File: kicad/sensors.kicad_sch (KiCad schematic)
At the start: 52 parts, among them J1 Bus_PCI_Express_x1, J4 Conn_01x02, J6 USB_C_Receptacle_USB2.0_16P, U2 RP2040, U4 W25Q128JVP, U5 BMP388, U8 BNO055, U9 MCP25625T-E/ML, X1 ABM8-272-T3, Y1 ABS07-32.768KHZ-T, Y2 X322516MLB4SI

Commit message: Update board to 0.2.0
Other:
- note added: "Sensor module 0.2.0"
- note removed: "Sensor module 0.1.0"
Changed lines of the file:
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@@
 		)
 	)
-	(text "Sensor module 0.1.0"
+	(text "Sensor module 0.2.0"
 		(exclude_from_sim no)
 		(at 493.014 386.842 0)

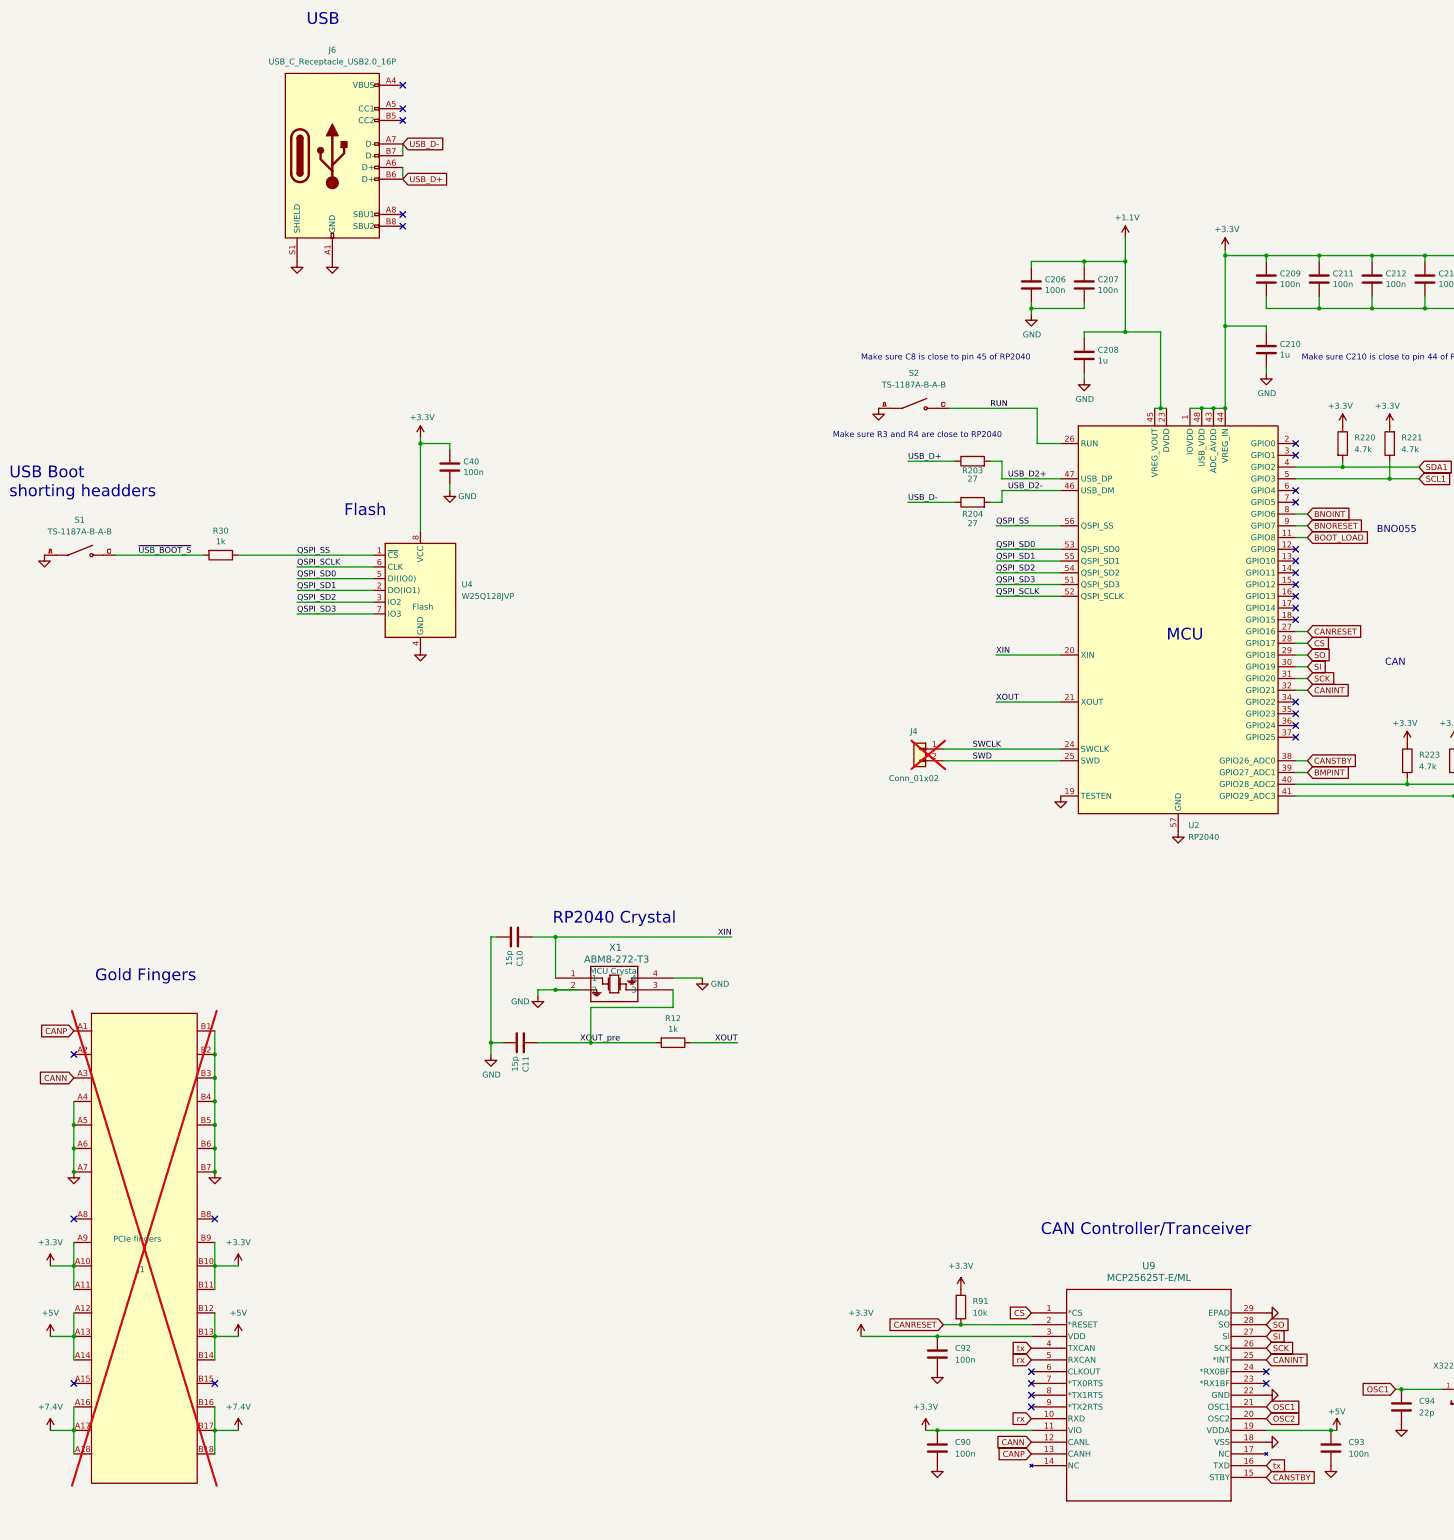
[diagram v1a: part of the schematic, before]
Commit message: add USBC resistors, power status LEDs, silk screen indicator, change SPI pins
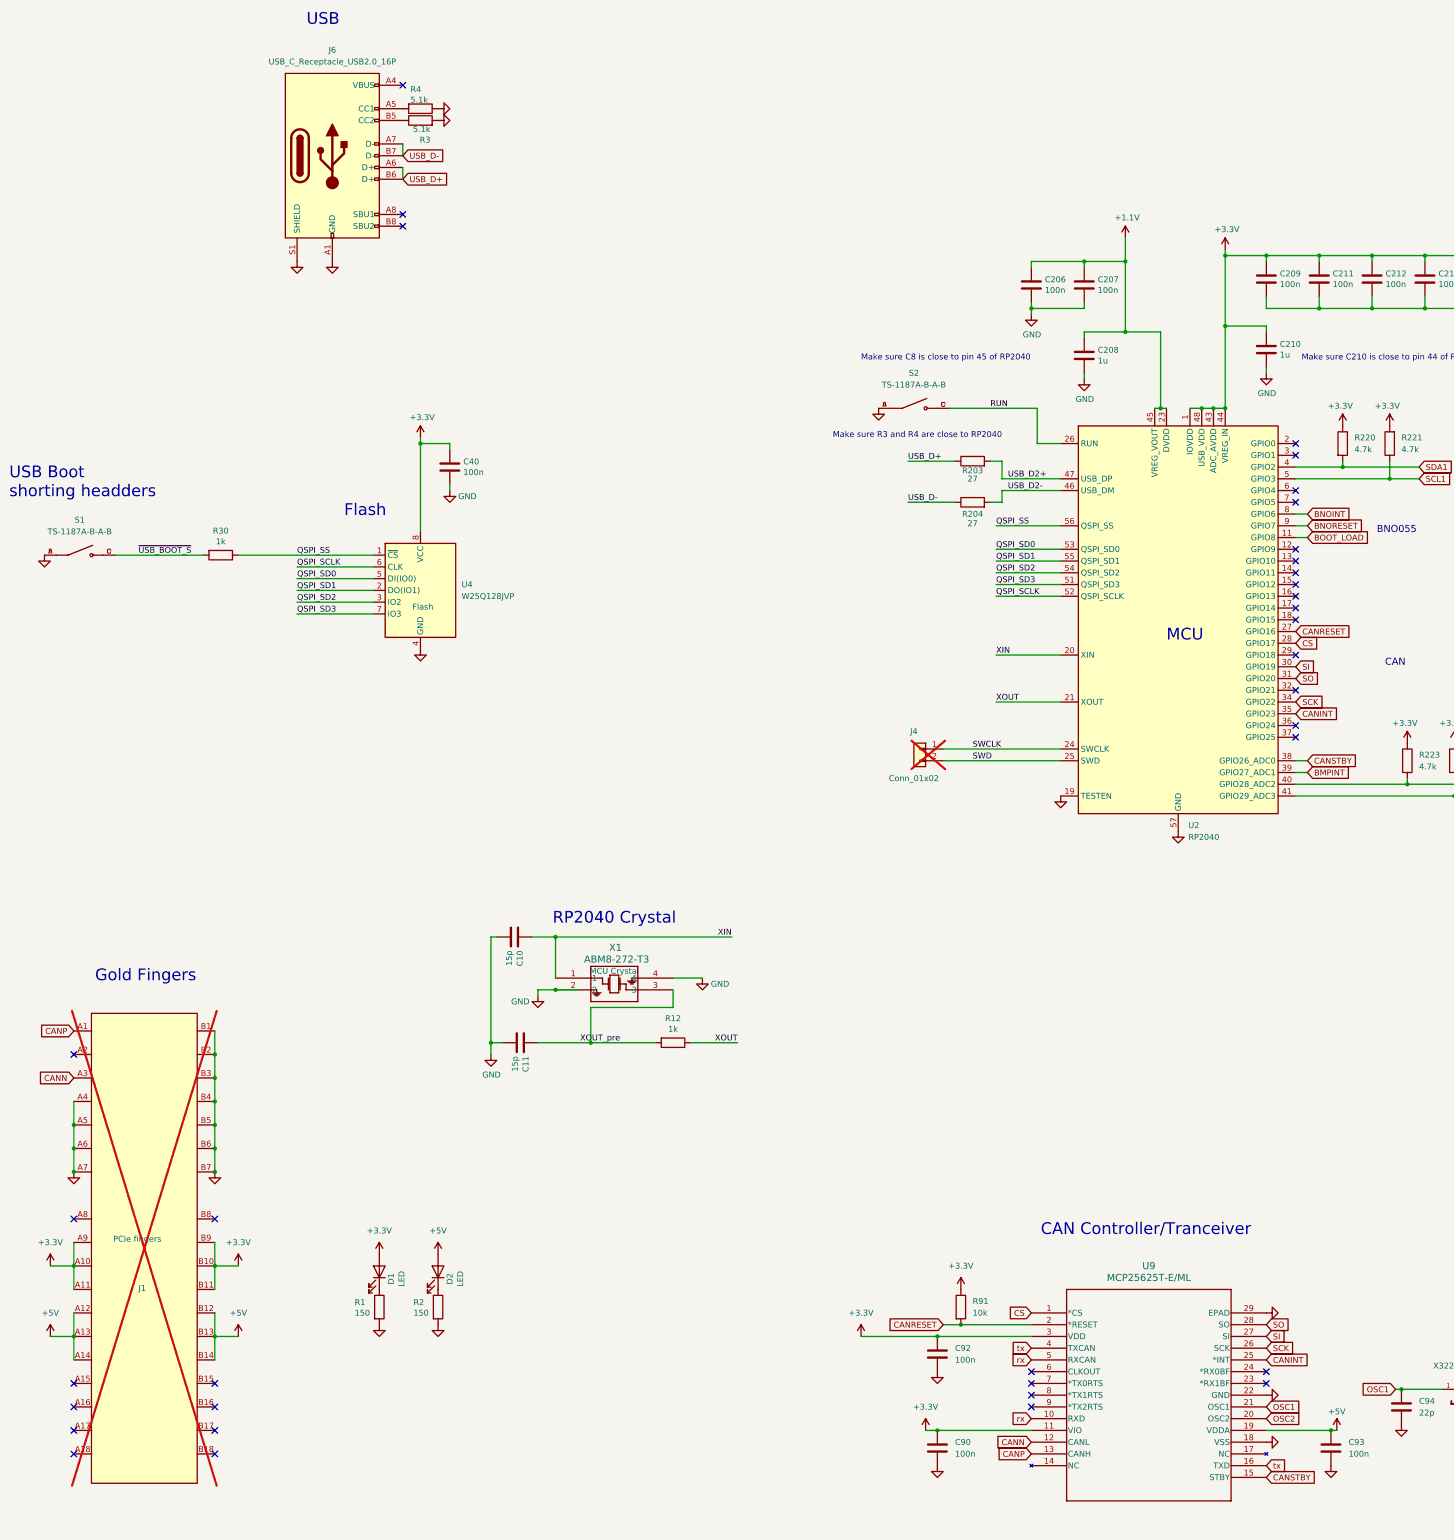
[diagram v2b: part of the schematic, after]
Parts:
- added D1, D2: LED, LED_SMD:LED_0603_1608Metric, symbol Device:LED
- added R1, R2: 150, Resistor_SMD:R_0603_1608Metric, symbol Device:R
- added R3, R4: 5.1k, Resistor_SMD:R_0603_1608Metric, symbol Device:R
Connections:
- net +3.3V: now also D1.2 (A)
- net +5V: now also D2.2 (A)
- net CANINT: now also U2.35 (GPIO23); no longer U2.32 (GPIO21)
- net GND: now also R1.2, R2.2, R3.2, R4.1
- net SCK: now also U2.34 (GPIO22); no longer U2.31 (GPIO20)
- net SO: now also U2.31 (GPIO20); no longer U2.29 (GPIO18)
- net at J6.A5 (CC1): now also R4.2
- net at J6.B5 (CC2): now also R3.1
- removed net +7.4V: J1.A16 (PERp0), J1.A17 (PERn0), J1.A18 (GND), J1.B16 (GND), J1.B17 (~{PRSNT2}), J1.B18 (GND)
- new net: D2.1 (K), R2.1
- new net: D1.1 (K), R1.1
- no-connect marks 31 -> 35

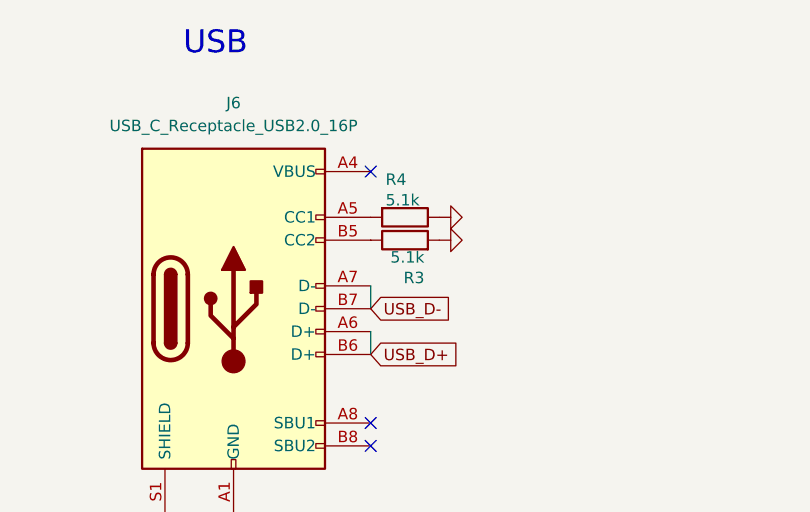
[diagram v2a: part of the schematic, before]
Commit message: update BOM, generate new production files
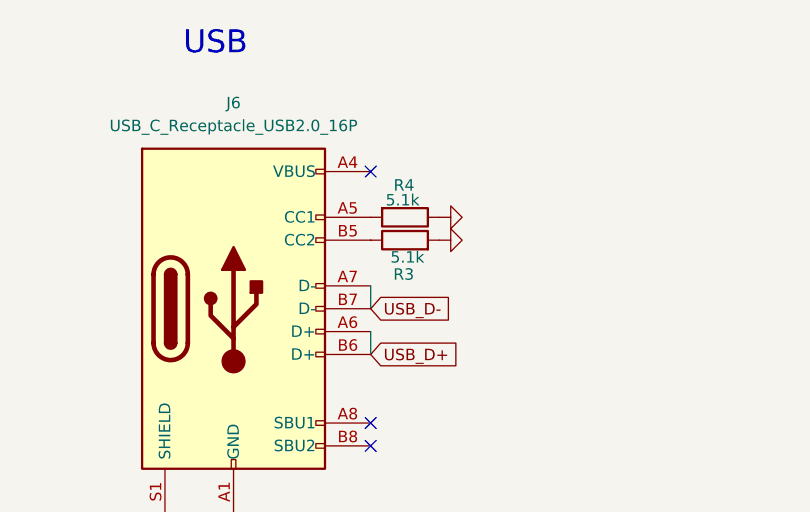
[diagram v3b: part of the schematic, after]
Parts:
- R3, R4: footprint Resistor_SMD:R_0603_1608Metric -> Resistor_SMD:R_0402_1005Metric; JLC Link https://jlcpcb.com/partdetail/23535-0603WAF1500T5E/C22808 -> https://jlcpcb.com/partdetail/26648-0402WGF5101TCE/C25905; LCSC Part # C22808 -> C25905; info 150 ohm -> 5.1k ohm; price C$0.0013 -> C$0.0006
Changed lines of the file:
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@@
 		(dnp no)
 		(property "Reference" "R3"
-			(at 138.049 77.851 90)
+			(at 136.906 77.47 90)
 			(effects
 				(font
@@
 			)
 		)
-		(property "Footprint" "Resistor_SMD:R_0603_1608Metric"
+		(property "Footprint" "Resistor_SMD:R_0402_1005Metric"
 			(at 135.89 75.438 90)
 			(effects
@@
 			)
 		)
-		(property "JLC Link" "https://jlcpcb.com/partdetail/23535-0603WAF1500T5E/C22808"
+		(property "JLC Link" "https://jlcpcb.com/partdetail/26648-0402WGF5101TCE/C25905"
 			(at 135.89 73.66 0)
 			(effects
@@
 			)
 		)
-		(property "LCSC Part #" "C22808"
+		(property "LCSC Part #" "C25905"
 			(at 135.89 73.66 0)
 			(effects
@@
 			)
 		)
-		(property "info" "150 ohm"
+		(property "info" "5.1k ohm"
 			(at 135.89 73.66 0)
 			(effects
@@
 			)
 		)
-		(property "price" "C$0.0013 "
+		(property "price" "C$0.0006"
 			(at 135.89 73.66 0)
 			(effects
@@
 		(dnp no)
 		(property "Reference" "R4"
-			(at 133.731 66.929 90)
+			(at 134.62 67.564 90)
 			(effects
 				(font
@@
 			)
 		)
-		(property "Footprint" "Resistor_SMD:R_0603_1608Metric"
+		(property "Footprint" "Resistor_SMD:R_0402_1005Metric"
 			(at 135.89 69.342 90)
 			(effects
@@
 			)
 		)
-		(property "JLC Link" "https://jlcpcb.com/partdetail/23535-0603WAF1500T5E/C22808"
+		(property "JLC Link" "https://jlcpcb.com/partdetail/26648-0402WGF5101TCE/C25905"
 			(at 135.89 71.12 0)
 			(effects
@@
 			)
 		)
-		(property "LCSC Part #" "C22808"
+		(property "LCSC Part #" "C25905"
 			(at 135.89 71.12 0)
 			(effects
@@
 			)
 		)
-		(property "info" "150 ohm"
+		(property "info" "5.1k ohm"
 			(at 135.89 71.12 0)
 			(effects
@@
 			)
 		)
-		(property "price" "C$0.0013 "
+		(property "price" "C$0.0006"
 			(at 135.89 71.12 0)
 			(effects

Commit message: update to kicad 9, update LED resistors
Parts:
- R1, R2: value 150 -> 1.5k

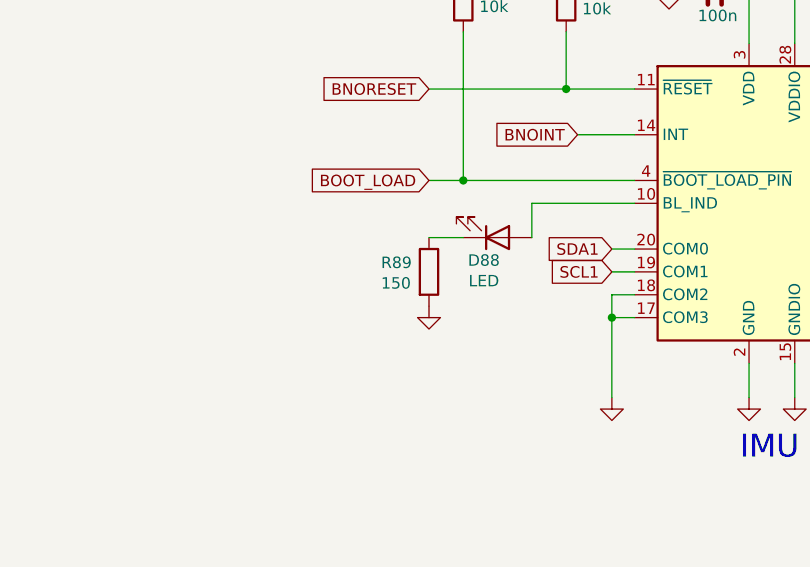
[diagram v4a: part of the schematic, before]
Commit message: move LEDs and text to bottom update to 0.2.1
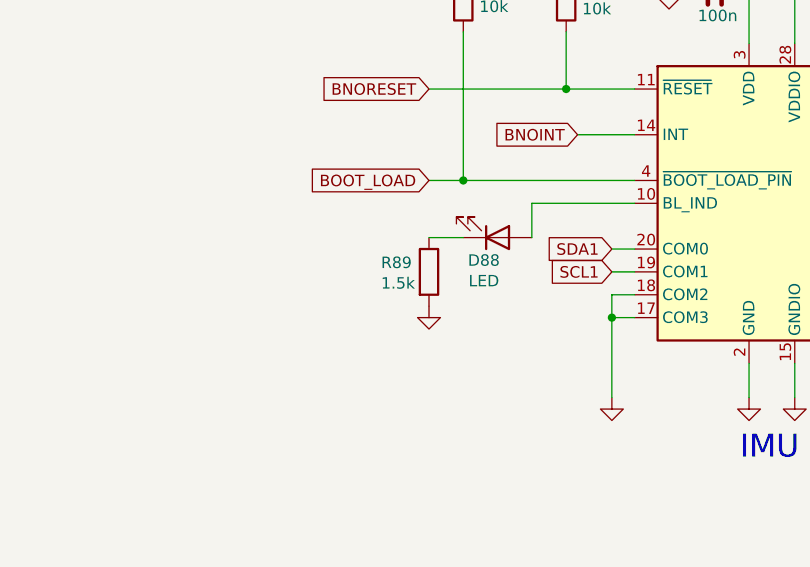
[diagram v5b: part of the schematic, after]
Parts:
- R89: value 150 -> 1.5k
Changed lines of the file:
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@@
 			)
 		)
-		(property "Value" "150"
+		(property "Value" "1.5k"
 			(at 422.656 300.99 0)
 			(effects
